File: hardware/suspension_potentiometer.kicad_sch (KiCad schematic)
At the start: 12 parts

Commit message: Add the Cube project
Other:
- note added: "5k"
- note removed: "<"
- note removed: "External connector"
- note removed: "POT 5k"
- note removed: "TODO: Separate power rail for external stuff"
- moved on the sheet: C?, R?

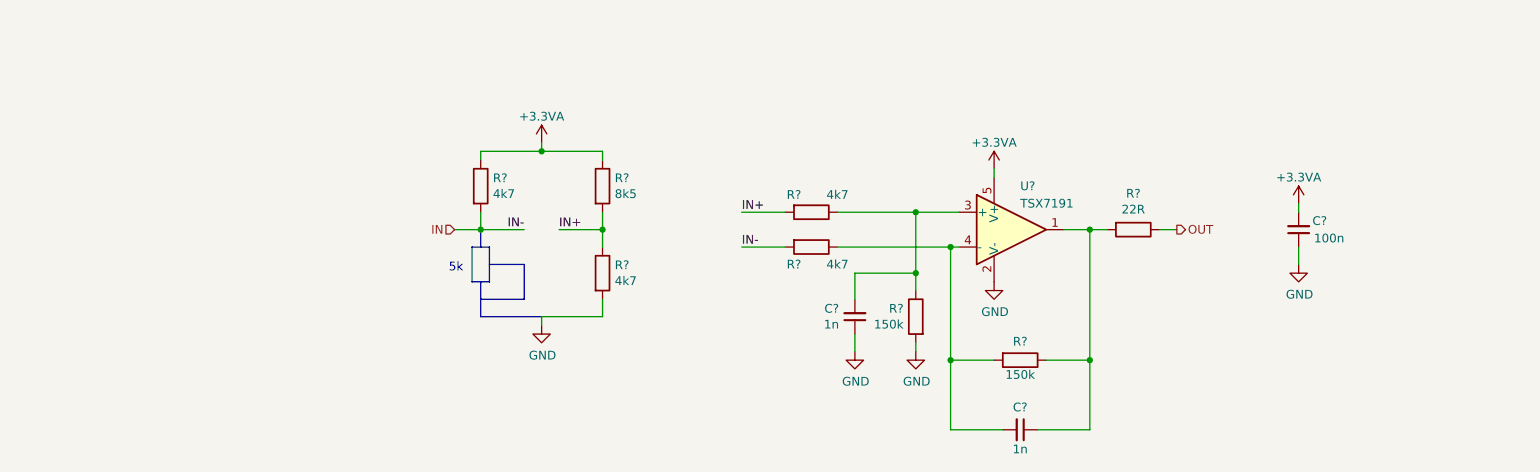
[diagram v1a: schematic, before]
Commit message: Improve the schematic
- add anti-aliasing filters
- rearrange the main connector signals
- improve the power filtering
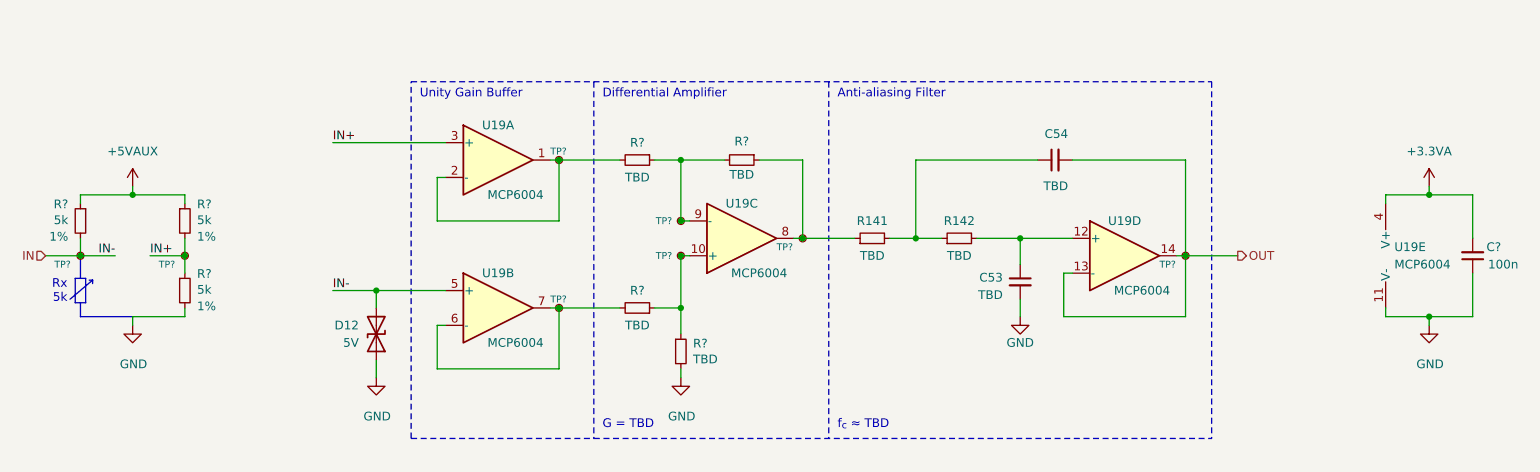
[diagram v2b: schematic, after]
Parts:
- removed C? (x2): 1n, Capacitor_SMD:C_0603_1608Metric, symbol Device:C_Small
- removed R? (x2): 4k7, Resistor_SMD:R_0603_1608Metric, symbol Device:R
- removed R?: 22R, Resistor_SMD:R_0603_1608Metric, symbol Device:R
- removed U?: TSX7191, Package_TO_SOT_SMD:SOT-23-5, symbol Amplifier_Operational:OPA340NA
- added C53, C54: TBD, Capacitor_SMD:C_0603_1608Metric_Pad1.08x0.95mm_HandSolder, symbol Device:C_Small
- added D12: 5V, symbol Device:D_TVS
- added R141, R142: TBD, Resistor_SMD:R_0603_1608Metric_Pad0.98x0.95mm_HandSolder, symbol Device:R_Small
- added R? (x2): 5k, Resistor_SMD:R_0603_1608Metric, symbol Device:R_Small
- added TP? (x8): TestPoint_Small, TestPoint:TestPoint_Pad_D1.0mm, symbol Connector:TestPoint_Small
- added U19: MCP6004, symbol Amplifier_Operational:MCP6004
- R? (x2): value 150k -> TBD; symbol Device:R -> Device:R_Small
- R? (x2): value 4k7 -> TBD; symbol Device:R -> Device:R_Small
- R?: value 8k5 -> 5k; symbol Device:R -> Device:R_Small; Tolerance (none) -> 1%
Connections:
- net +3.3VA: now also U19.4 (V+); no longer R?.1
- net GND: now also C53.2, D12.1 (A1), R?.2, U19.11 (V-)
- net IN: now also D12.2 (A2), R?.2, TP?.1, U19.5 (+); no longer R?.2
- net IN+: now also R?.1, TP?.1, U19.3 (+); no longer R?.2
- net OUT: now also C54.2, TP?.1, U19.13 (-), U19.14
- net at R?.1: now also R?.1, TP?.1, U19.10 (+); no longer R?.1
- net at R?.1: now also R141.1, TP?.1, U19.8
- net at R?.2: now also R?.1, TP?.1, U19.9 (-); no longer R?.1
- new net: R?.2, TP?.1, U19.6 (-), U19.7
- new net: C54.1, R141.2, R142.1
- new net: R?.2, TP?.1, U19.1, U19.2 (-)
- new net: C53.1, R142.2, U19.12 (+)
- new net +5VAUX: R?.1, R?.1
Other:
- note added: "Anti-aliasing Filter"
- note added: "Differential Amplifier"
- note added: "G = TBD"
- note added: "Rx 5k"
- note added: "Unity Gain Buffer"
- note added: "f_{c} ≈ TBD"
- note removed: "5k"
- moved on the sheet: C?, R?

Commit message: Set component values
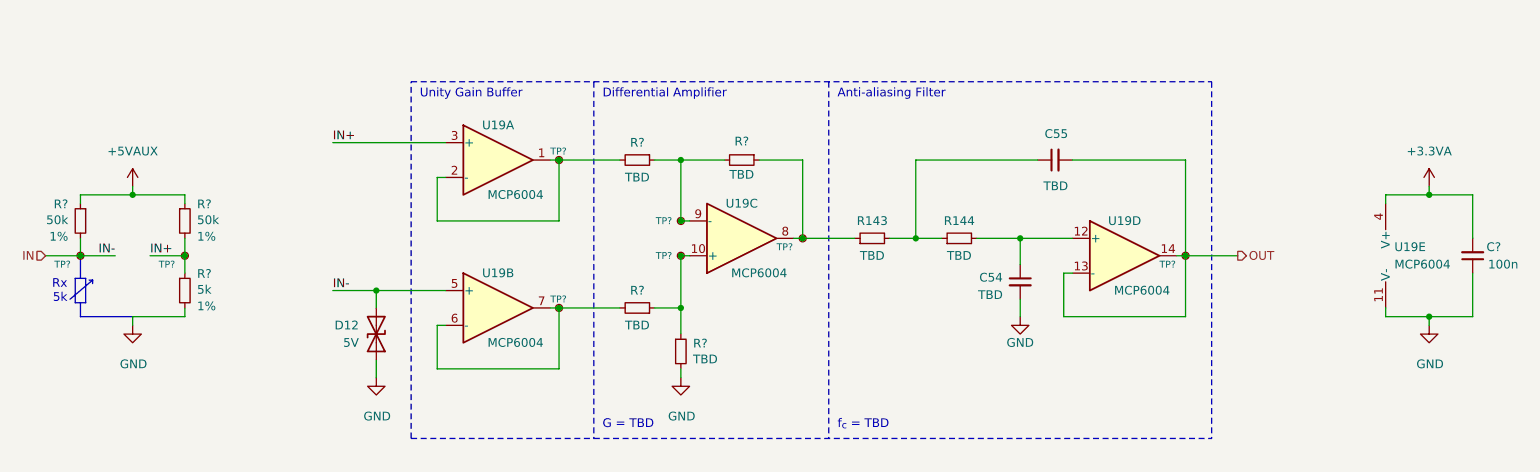
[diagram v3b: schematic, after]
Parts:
- C54: renamed from C53; footprint Capacitor_SMD:C_0603_1608Metric_Pad1.08x0.95mm_HandSolder -> Capacitor_SMD:C_0603_1608Metric
- C55: renamed from C54; footprint Capacitor_SMD:C_0603_1608Metric_Pad1.08x0.95mm_HandSolder -> Capacitor_SMD:C_0603_1608Metric
- R143: renamed from R141; footprint Resistor_SMD:R_0603_1608Metric_Pad0.98x0.95mm_HandSolder -> Resistor_SMD:R_0603_1608Metric
- R144: renamed from R142; footprint Resistor_SMD:R_0603_1608Metric_Pad0.98x0.95mm_HandSolder -> Resistor_SMD:R_0603_1608Metric
- R? (x2): value 5k -> 50k
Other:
- note added: "f_{c} = TBD"
- note removed: "f_{c} ≈ TBD"
- title: (none) -> Suspension Potentiometer

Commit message: Improve the schematic according to the feedback
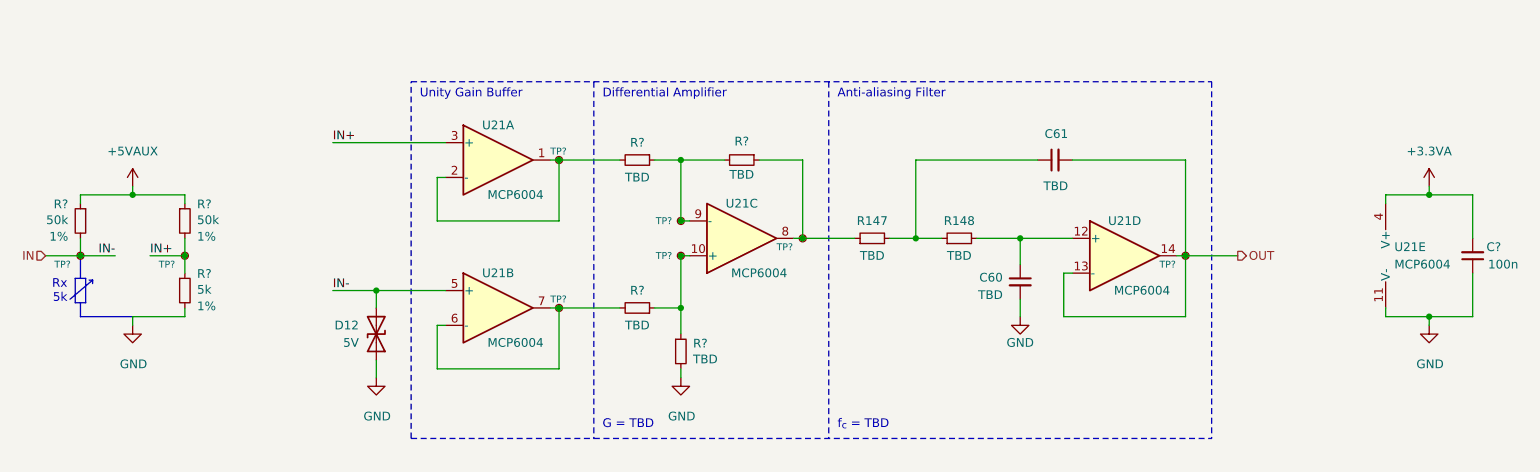
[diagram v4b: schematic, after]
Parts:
- renumbered C54 to C60, C55 to C61, R143 to R147, R144 to R148, U19 to U21

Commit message: Add high-side drivers to the fans and pumps
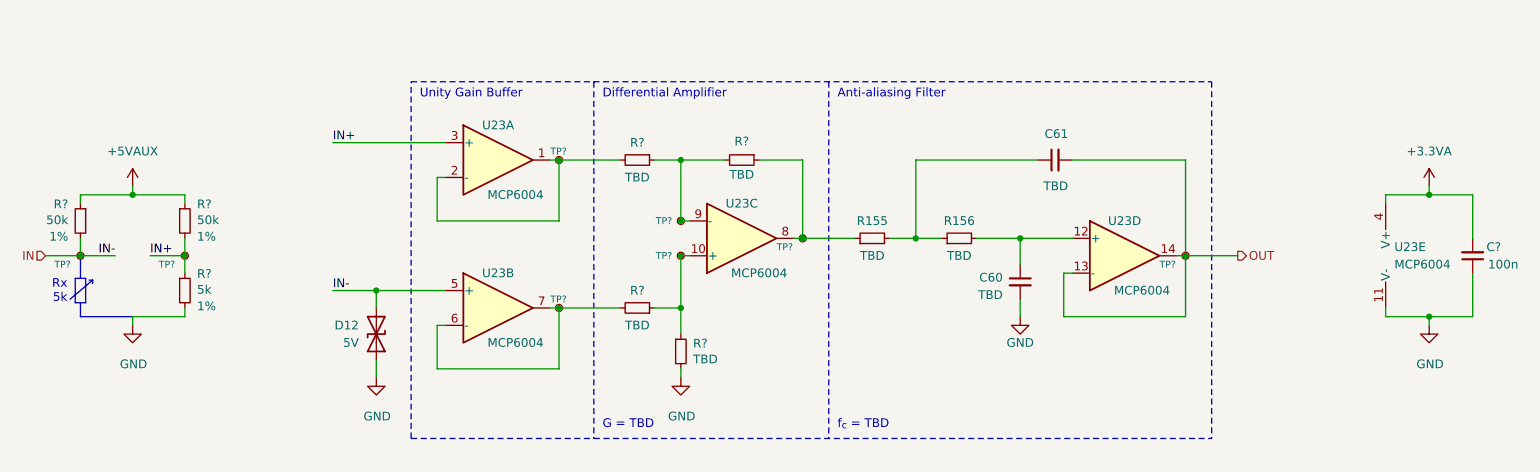
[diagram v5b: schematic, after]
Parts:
- renumbered R147 to R155, R148 to R156, U21 to U23

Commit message: Use in-amps
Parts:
- removed C60, C61: TBD, Capacitor_SMD:C_0603_1608Metric, symbol Device:C_Small
- removed C?: 100n, Capacitor_SMD:C_0603_1608Metric, symbol Device:C_Small
- removed D12: 5V, symbol Device:D_TVS
- removed R155, R156, R? (x4): TBD, Resistor_SMD:R_0603_1608Metric, symbol Device:R_Small
- removed TP? (x6): TestPoint_Small, TestPoint:TestPoint_Pad_D1.0mm, symbol Connector:TestPoint_Small
- removed U23: MCP6004, symbol Amplifier_Operational:MCP6004
- added C? (x2): 100n, Capacitor_SMD:C_0603_1608Metric, symbol Device:C_Small
- added C? (x2): TBD, Capacitor_SMD:C_0603_1608Metric, symbol Device:C_Small
- added D14: 5V, symbol Device:D_TVS
- added NT4: NetTie_2, symbol Device:NetTie_2
- added R? (x4): TBD, Resistor_SMD:R_0603_1608Metric, symbol Device:R_Small
- added TP? (x4): TestPoint_Small, TestPoint:TestPoint_Pad_D1.0mm, symbol Connector:TestPoint_Small
- added U?: MCP6001, Package_TO_SOT_SMD:SOT-23-5, symbol Amplifier_Operational:MCP6001-OT
- added U?: MCP6N11-005, Package_DFN_QFN:TDFN-8-1EP_3x2mm_P0.5mm_EP1.80x1.65mm, symbol MCP6N11:MCP6N11
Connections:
- net +3.3VA: now also C?.1, C?.1, U?.5 (V+), U?.7 (V+), U?.8 (EN)
- net GND: now also C?.2, C?.2, C?.2, D14.1 (A1), R?.1, U?.2 (V-), U?.4 (V-), U?.5 (RF), U?.9 (EP)
- net IN: now also NT4.1; no longer R?.2, TP?.1
- net IN+: now also TP?.1, U?.2 (-)
- net OUT: now also C?.2, TP?.1, U?.1, U?.4 (-)
- new net: C?.1, R?.2, U?.3 (+)
- new net: R?.1, R?.2, TP?.1, U?.6
- new net: C?.1, R?.1, R?.2
- new net: R?.1, R?.2, U?.1 (FG)
- new net IN-: D14.2 (A2), NT4.2, R?.2, TP?.1, TP?.1, U?.3 (+)
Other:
- note added: "Instrumentation Amplifier"
- note removed: "Differential Amplifier"
- note removed: "Unity Gain Buffer"

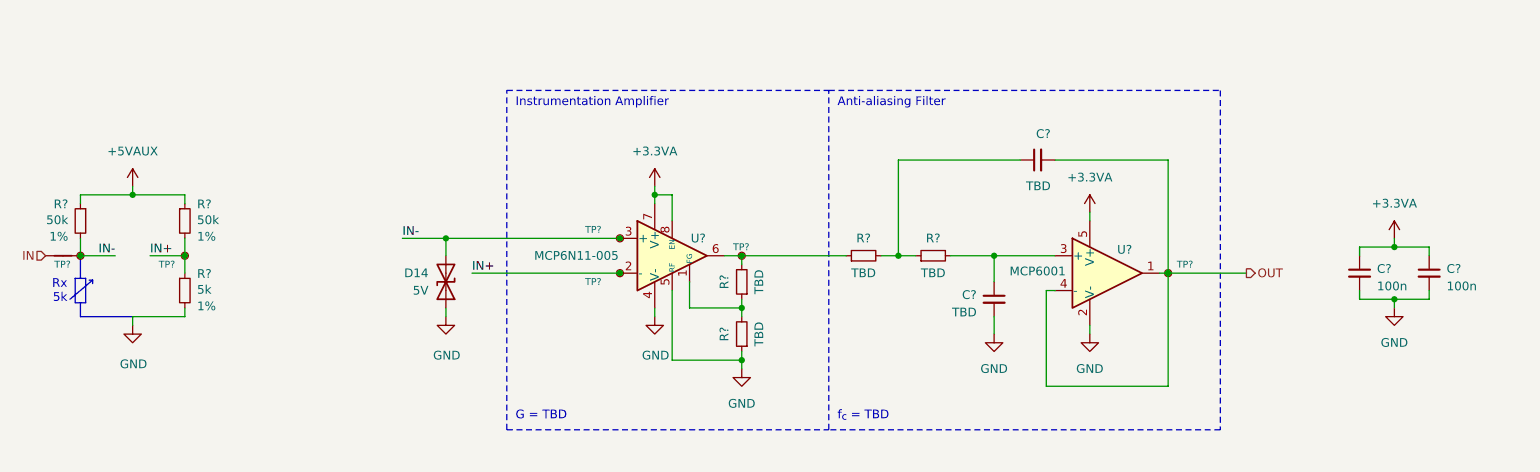
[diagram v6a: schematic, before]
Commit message: Improve the diagram based on the feedback
- add an input LC filter
- remove the USB connector
- add a programmer connector
- move optocouplers into a subsheet
- add a suspension tension meter IC
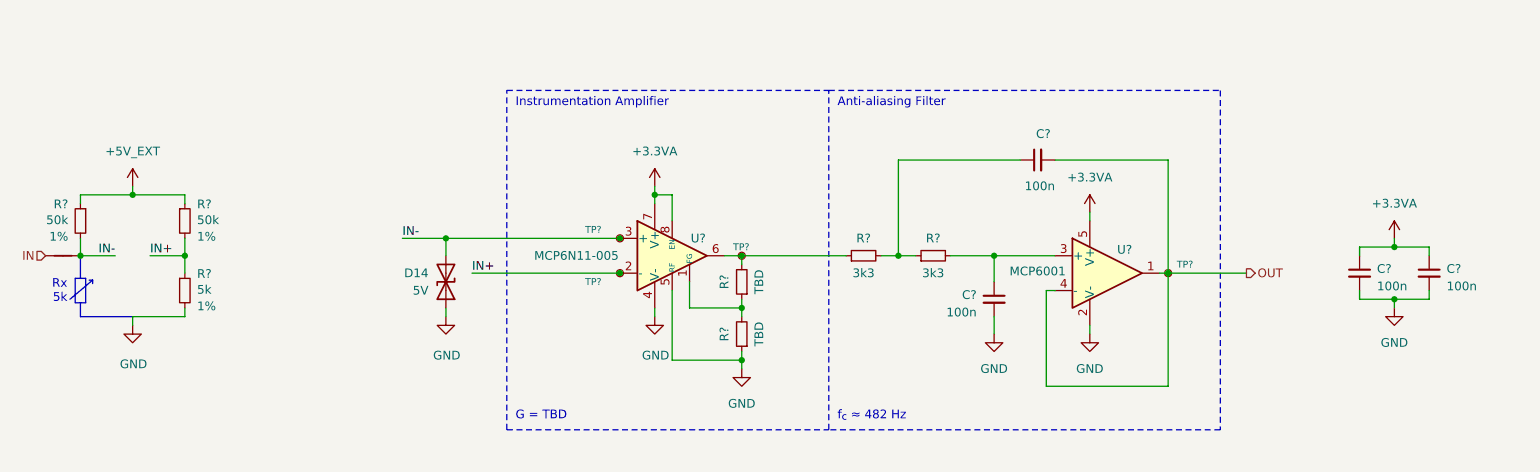
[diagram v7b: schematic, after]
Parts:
- removed TP? (x2): TestPoint_Small, TestPoint:TestPoint_Pad_D1.0mm, symbol Connector:TestPoint_Small
- C? (x2): value TBD -> 100n
- D14: footprint (none) -> Diode_SMD:D_SOD-523; Component (none) -> PESD5V0V1BB-QX
- NT4: footprint (none) -> NetTie:NetTie-2_SMD_Pad0.5mm
- R? (x2): value TBD -> 3k3
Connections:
- net +5VAUX renamed +5V_EXT
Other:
- note added: "f_{c} ≈ 482 Hz"
- note removed: "f_{c} = TBD"
